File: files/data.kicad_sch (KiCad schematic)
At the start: 2 parts, among them J1 VLB_slot

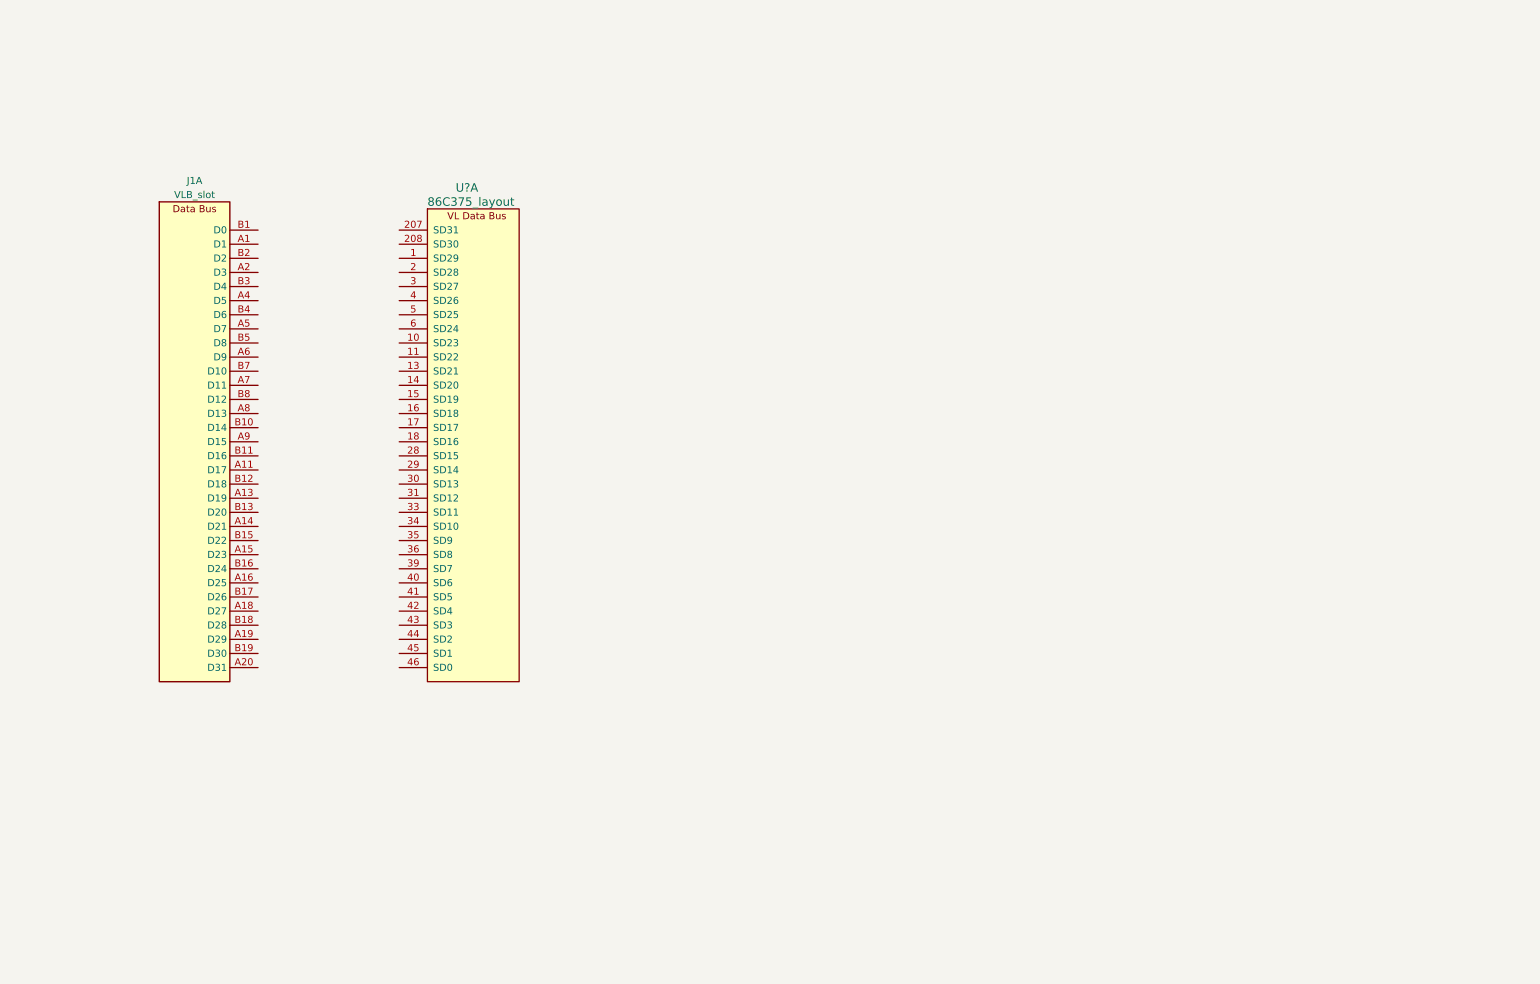
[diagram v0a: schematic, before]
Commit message: work on the memory bus, fixed symbols
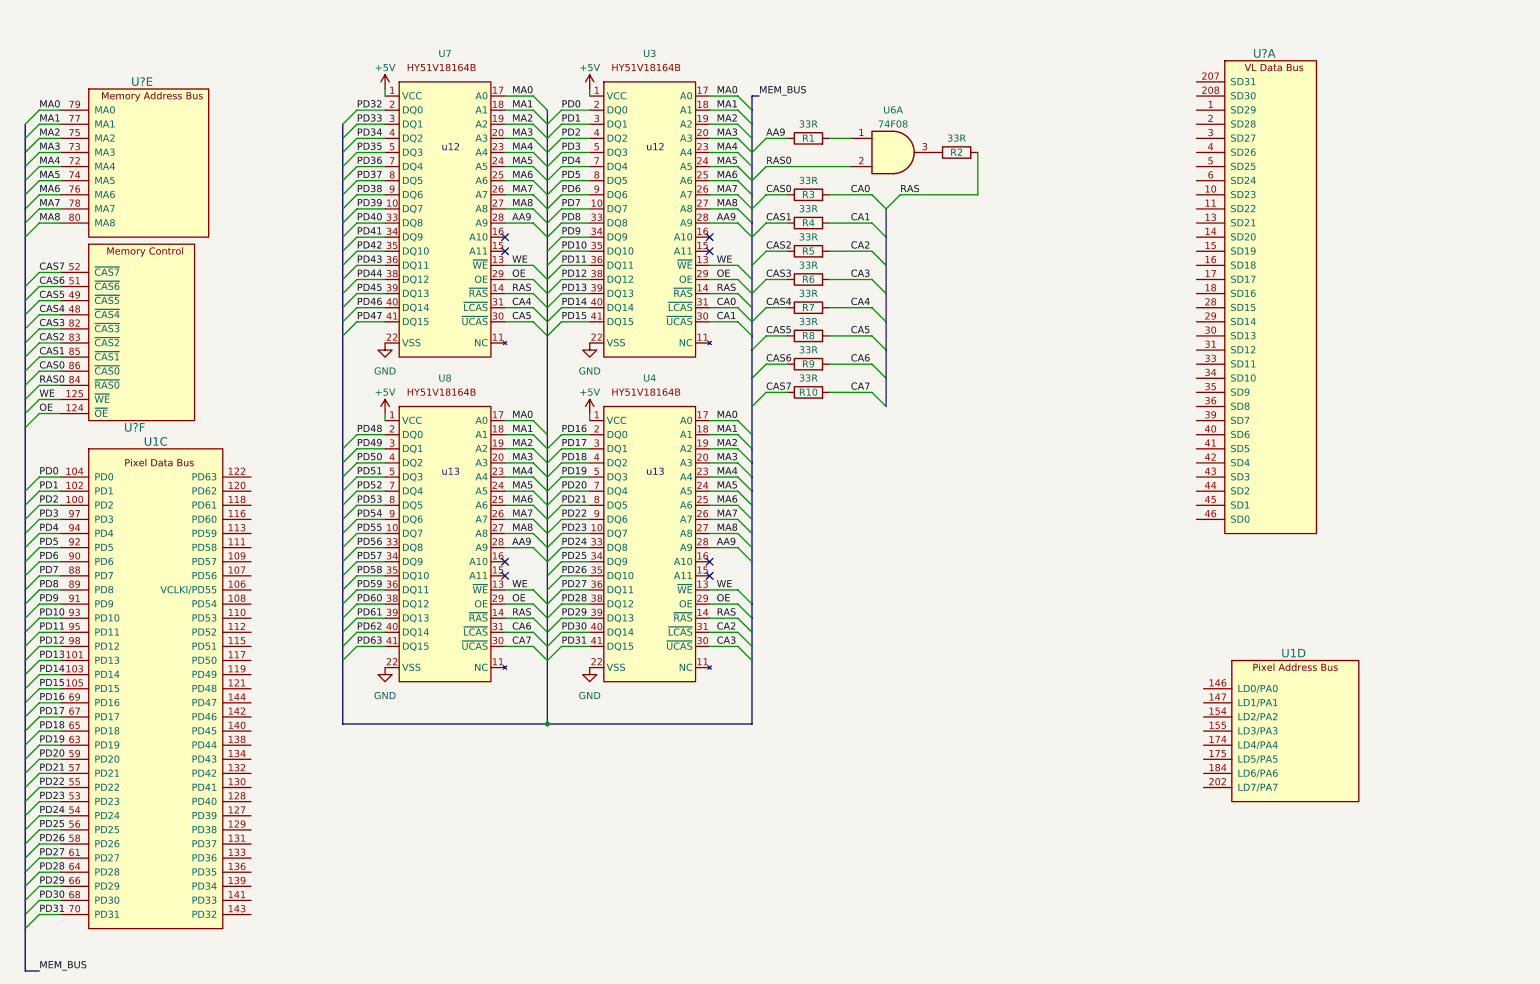
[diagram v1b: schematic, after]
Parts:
- removed J1: VLB_slot, symbol virge:VLB_slot
- added R1, R10, R2, R3, R4, R5, R6, R7, R8, R9: 33R, Resistor_SMD:R_0805_2012Metric, symbol Device:R
- added U1, U? (x2): 86C375_layout, Package_QFP:PQFP-208_28x28mm_P0.5mm, symbol virge:86C375_layout
- added U3, U4, U7, U8: ~, symbol virge:HY51V18164B
- added U6: 74F08, Package_SO:SOIC-14_3.9x8.7mm_P1.27mm, symbol 74xx:74LS08
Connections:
- new net: U7.11 (NC), U7.12 (NC), U7.32 (NC)
- new net: R1.2, U6.1
- new net: R2.1, U6.3
- new net: U4.11 (NC), U4.12 (NC), U4.32 (NC)
- new net: U3.11 (NC), U3.12 (NC), U3.32 (NC)
- new net: U8.11 (NC), U8.12 (NC), U8.32 (NC)
- new net +5V: U3.1 (VCC), U3.21 (VCC), U3.6 (VCC), U4.1 (VCC), U4.21 (VCC), U4.6 (VCC), U7.1 (VCC), U7.21 (VCC), U7.6 (VCC), U8.1 (VCC), U8.21 (VCC), U8.6 (VCC)
- new net AA9: R1.1, U3.28 (A9), U4.28 (A9), U7.28 (A9), U8.28 (A9)
- new net CA0: R3.2, U3.31 (~{LCAS})
- new net CA1: R4.2, U3.30 (~{UCAS})
- new net CA2: R5.2, U4.31 (~{LCAS})
- new net CA3: R6.2, U4.30 (~{UCAS})
- new net CA4: R7.2, U7.31 (~{LCAS})
- new net CA5: R8.2, U7.30 (~{UCAS})
- new net CA6: R9.2, U8.31 (~{LCAS})
- new net CA7: R10.2, U8.30 (~{UCAS})
- new net CAS0: R3.1, U?.86 (~{CAS0})
- new net CAS1: R4.1, U?.85 (~{CAS1})
- new net CAS2: R5.1, U?.83 (~{CAS2})
- new net CAS3: R6.1, U?.82 (~{CAS3})
- new net CAS4: R7.1, U?.48 (~{CAS4})
- new net CAS5: R8.1, U?.49 (~{CAS5})
- new net CAS6: R9.1, U?.51 (~{CAS6})
- new net CAS7: R10.1, U?.52 (~{CAS7})
- new net GND: U3.22 (VSS), U3.37 (VSS), U3.42 (VSS), U4.22 (VSS), U4.37 (VSS), U4.42 (VSS), U7.22 (VSS), U7.37 (VSS), U7.42 (VSS), U8.22 (VSS), U8.37 (VSS), U8.42 (VSS)
- new net MA0: U3.17 (A0), U4.17 (A0), U7.17 (A0), U8.17 (A0), U?.79 (MA0)
- new net MA1: U3.18 (A1), U4.18 (A1), U7.18 (A1), U8.18 (A1), U?.77 (MA1)
- new net MA2: U3.19 (A2), U4.19 (A2), U7.19 (A2), U8.19 (A2), U?.75 (MA2)
- new net MA3: U3.20 (A3), U4.20 (A3), U7.20 (A3), U8.20 (A3), U?.73 (MA3)
- new net MA4: U3.23 (A4), U4.23 (A4), U7.23 (A4), U8.23 (A4), U?.72 (MA4)
- new net MA5: U3.24 (A5), U4.24 (A5), U7.24 (A5), U8.24 (A5), U?.74 (MA5)
- new net MA6: U3.25 (A6), U4.25 (A6), U7.25 (A6), U8.25 (A6), U?.76 (MA6)
- new net MA7: U3.26 (A7), U4.26 (A7), U7.26 (A7), U8.26 (A7), U?.78 (MA7)
- new net MA8: U3.27 (A8), U4.27 (A8), U7.27 (A8), U8.27 (A8), U?.80 (MA8)
- new net OE: U3.29 (OE), U4.29 (OE), U7.29 (OE), U8.29 (OE), U?.124 (~{OE})
- new net PD0: U1.104 (PD0), U3.2 (DQ0)
- new net PD1: U1.102 (PD1), U3.3 (DQ1)
- new net PD10: U1.93 (PD10), U3.35 (DQ10)
- new net PD11: U1.95 (PD11), U3.36 (DQ11)
- new net PD12: U1.98 (PD12), U3.38 (DQ12)
- new net PD13: U1.101 (PD13), U3.39 (DQ13)
- new net PD14: U1.103 (PD14), U3.40 (DQ14)
- new net PD15: U1.105 (PD15), U3.41 (DQ15)
- new net PD16: U1.69 (PD16), U4.2 (DQ0)
- new net PD17: U1.67 (PD17), U4.3 (DQ1)
- new net PD18: U1.65 (PD18), U4.4 (DQ2)
- new net PD19: U1.63 (PD19), U4.5 (DQ3)
- new net PD2: U1.100 (PD2), U3.4 (DQ2)
- new net PD20: U1.59 (PD20), U4.7 (DQ4)
- new net PD21: U1.57 (PD21), U4.8 (DQ5)
- new net PD22: U1.55 (PD22), U4.9 (DQ6)
- new net PD23: U1.53 (PD23), U4.10 (DQ7)
- new net PD24: U1.54 (PD24), U4.33 (DQ8)
- new net PD25: U1.56 (PD25), U4.34 (DQ9)
- new net PD26: U1.58 (PD26), U4.35 (DQ10)
- new net PD27: U1.61 (PD27), U4.36 (DQ11)
- new net PD28: U1.64 (PD28), U4.38 (DQ12)
- new net PD29: U1.66 (PD29), U4.39 (DQ13)
- new net PD3: U1.97 (PD3), U3.5 (DQ3)
- new net PD30: U1.68 (PD30), U4.40 (DQ14)
- new net PD31: U1.70 (PD31), U4.41 (DQ15)
- new net PD32: U7.2 (DQ0)
- new net PD33: U7.3 (DQ1)
- new net PD34: U7.4 (DQ2)
- new net PD35: U7.5 (DQ3)
- new net PD36: U7.7 (DQ4)
- new net PD37: U7.8 (DQ5)
- new net PD38: U7.9 (DQ6)
- new net PD39: U7.10 (DQ7)
- new net PD4: U1.94 (PD4), U3.7 (DQ4)
- new net PD40: U7.33 (DQ8)
- new net PD41: U7.34 (DQ9)
- new net PD42: U7.35 (DQ10)
- new net PD43: U7.36 (DQ11)
- new net PD44: U7.38 (DQ12)
- new net PD45: U7.39 (DQ13)
- new net PD46: U7.40 (DQ14)
- new net PD47: U7.41 (DQ15)
- new net PD48: U8.2 (DQ0)
- new net PD49: U8.3 (DQ1)
- new net PD5: U1.92 (PD5), U3.8 (DQ5)
- new net PD50: U8.4 (DQ2)
- new net PD51: U8.5 (DQ3)
- new net PD52: U8.7 (DQ4)
- new net PD53: U8.8 (DQ5)
- new net PD54: U8.9 (DQ6)
- new net PD55: U8.10 (DQ7)
- new net PD56: U8.33 (DQ8)
- new net PD57: U8.34 (DQ9)
- new net PD58: U8.35 (DQ10)
- new net PD59: U8.36 (DQ11)
- new net PD6: U1.90 (PD6), U3.9 (DQ6)
- new net PD60: U8.38 (DQ12)
- new net PD61: U8.39 (DQ13)
- new net PD62: U8.40 (DQ14)
- new net PD63: U8.41 (DQ15)
- new net PD7: U1.88 (PD7), U3.10 (DQ7)
- new net PD8: U1.89 (PD8), U3.33 (DQ8)
- new net PD9: U1.91 (PD9), U3.34 (DQ9)
- new net RAS: R2.2, U3.14 (~{RAS}), U4.14 (~{RAS}), U7.14 (~{RAS}), U8.14 (~{RAS})
- new net RAS0: U6.2, U?.84 (~{RAS0})
- new net WE: U3.13 (~{WE}), U4.13 (~{WE}), U7.13 (~{WE}), U8.13 (~{WE}), U?.125 (~{WE})
- no-connect marks 0 -> 8
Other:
- note added: "u12"
- note added: "u13"
- moved on the sheet: U?A

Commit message: changed memory chips, more progress
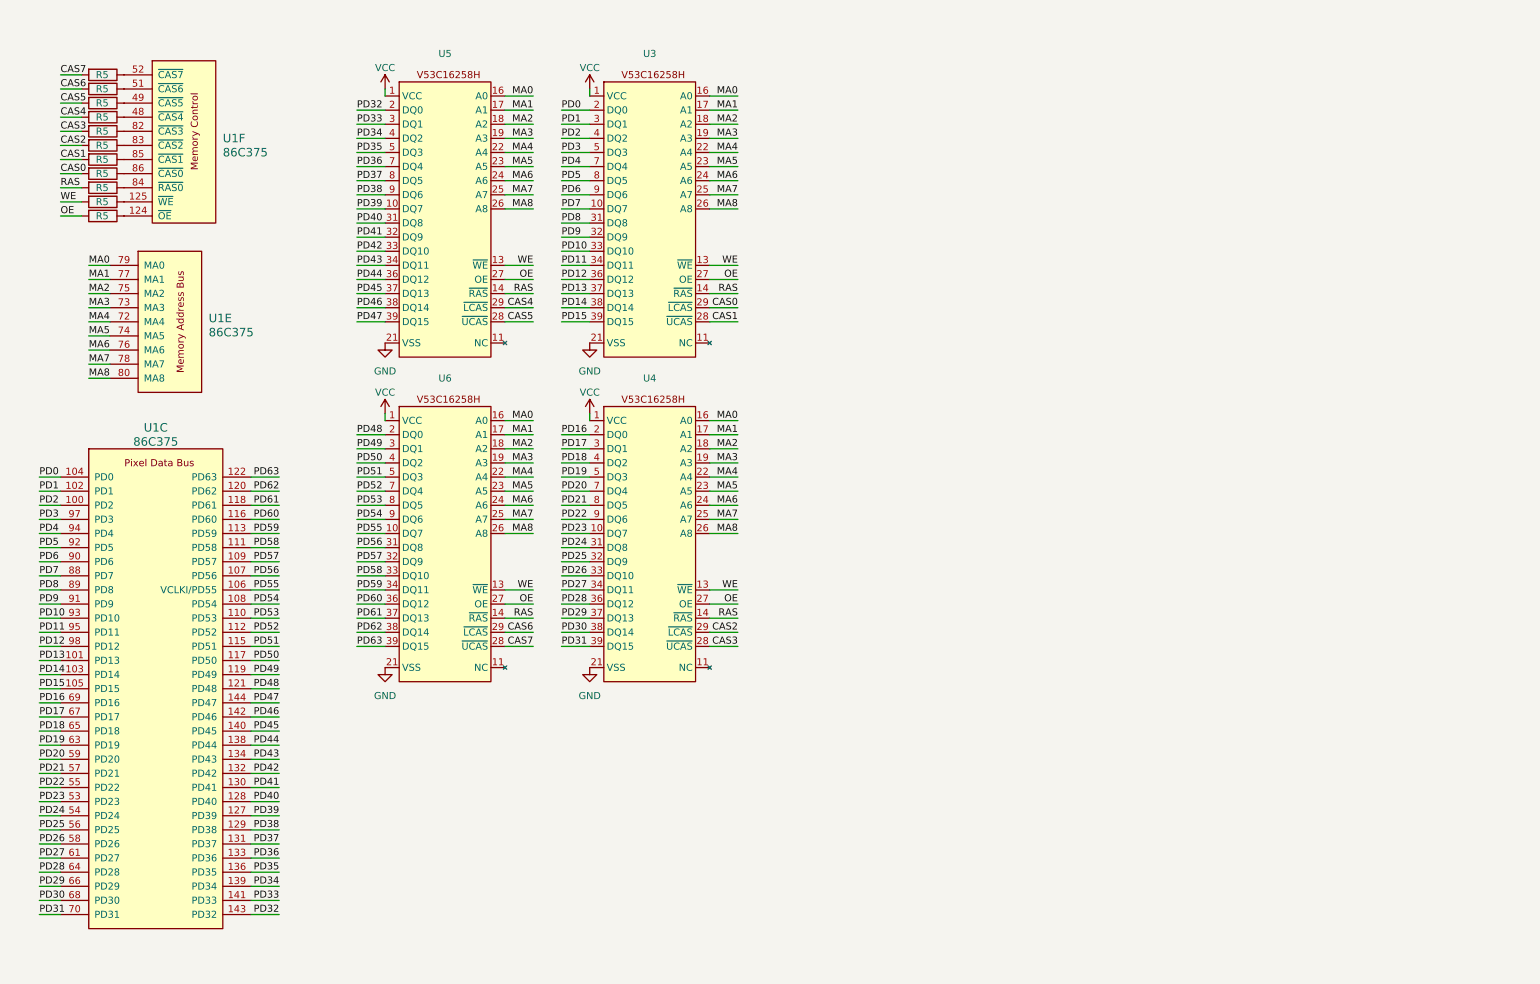
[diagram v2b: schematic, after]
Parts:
- removed R1, R10, R2, R3, R4, R5, R6, R7, R8, R9: 33R, Resistor_SMD:R_0805_2012Metric, symbol Device:R
- removed U1, U? (x3): 86C375_layout, Package_QFP:PQFP-208_28x28mm_P0.5mm, symbol virge:86C375_layout
- removed U6: 74F08, Package_SO:SOIC-14_3.9x8.7mm_P1.27mm, symbol 74xx:74LS08
- removed U7, U8: ~, symbol virge:HY51V18164B
- added R5 (x11): 33R, Resistor_SMD:R_0805_2012Metric_Pad1.20x1.40mm_HandSolder, symbol Device:R
- added U1: 86C375, Package_QFP:PQFP-208_28x28mm_P0.5mm, symbol virge:86C375
- added U5, U6: ~, VLB:SOJ-40_10.16x26.00mm_P1.27mm, symbol virge:HY51V18164B
- U3, U4: footprint (none) -> VLB:SOJ-40_10.16x26.00mm_P1.27mm
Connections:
- net CA0 is gone; now on net PD8: U3.31 (DQ8)
- net CA1 is gone; now on an unnamed net: U3.30 (NC)
- net CA2 is gone; now on net PD24: U4.31 (DQ8)
- net CA3 is gone; now on an unnamed net: U4.30 (NC)
- net CAS0: now also U3.29 (~{LCAS}), R5.2
- net CAS1: now also U3.28 (~{UCAS}), R5.2
- net CAS2: now also U4.29 (~{LCAS}), R5.2
- net CAS3: now also U4.28 (~{UCAS}), R5.2
- net CAS4: now also R5.2, U5.29 (~{LCAS})
- net CAS5: now also R5.2, U5.28 (~{UCAS})
- net CAS6: now also R5.2, U6.29 (~{LCAS})
- net CAS7: now also R5.2, U6.28 (~{UCAS})
- net GND: now also U3.21 (VSS), U3.35 (VSS), U3.40 (VSS), U4.21 (VSS), U4.35 (VSS), U4.40 (VSS), U5.21 (VSS), U5.35 (VSS), U5.40 (VSS), U6.21 (VSS), U6.35 (VSS), U6.40 (VSS); no longer U3.22 (VSS), U3.37 (VSS), U3.42 (VSS), U4.22 (VSS), U4.37 (VSS), U4.42 (VSS)
- net MA0: now also U3.16 (A0), U4.16 (A0), U1.79 (MA0), U5.16 (A0), U6.16 (A0); no longer U3.17 (A0), U4.17 (A0)
- net MA1: now also U3.17 (A1), U4.17 (A1), U1.77 (MA1), U5.17 (A1), U6.17 (A1); no longer U3.18 (A1), U4.18 (A1)
- net MA2: now also U3.18 (A2), U4.18 (A2), U1.75 (MA2), U5.18 (A2), U6.18 (A2); no longer U3.19 (A2), U4.19 (A2)
- net MA3: now also U3.19 (A3), U4.19 (A3), U1.73 (MA3), U5.19 (A3), U6.19 (A3); no longer U3.20 (A3), U4.20 (A3)
- net MA4: now also U3.22 (A4), U4.22 (A4), U1.72 (MA4), U5.22 (A4), U6.22 (A4); no longer U3.23 (A4), U4.23 (A4)
- net MA5: now also U3.23 (A5), U4.23 (A5), U1.74 (MA5), U5.23 (A5), U6.23 (A5); no longer U3.24 (A5), U4.24 (A5)
- net MA6: now also U3.24 (A6), U4.24 (A6), U1.76 (MA6), U5.24 (A6), U6.24 (A6); no longer U3.25 (A6), U4.25 (A6)
- net MA7: now also U3.25 (A7), U4.25 (A7), U1.78 (MA7), U5.25 (A7), U6.25 (A7); no longer U3.26 (A7), U4.26 (A7)
- net MA8: now also U3.26 (A8), U4.26 (A8), U1.80 (MA8), U5.26 (A8), U6.26 (A8); no longer U3.27 (A8), U4.27 (A8)
- net OE: now also U3.27 (OE), U4.27 (OE), R5.2, U5.27 (OE), U6.27 (OE); no longer U3.29 (OE), U4.29 (OE)
- net PD0: now also U1.104 (PD0)
- net PD1: now also U1.102 (PD1)
- net PD10: now also U3.33 (DQ10), U1.93 (PD10); no longer U3.35 (DQ10)
- net PD11: now also U3.34 (DQ11), U1.95 (PD11); no longer U3.36 (DQ11)
- net PD12: now also U3.36 (DQ12), U1.98 (PD12); no longer U3.38 (DQ12)
- net PD13: now also U3.37 (DQ13), U1.101 (PD13); no longer U3.39 (DQ13)
- net PD14: now also U3.38 (DQ14), U1.103 (PD14); no longer U3.40 (DQ14)
- net PD15: now also U3.39 (DQ15), U1.105 (PD15); no longer U3.41 (DQ15)
- net PD16: now also U1.69 (PD16)
- net PD17: now also U1.67 (PD17)
- net PD18: now also U1.65 (PD18)
- net PD19: now also U1.63 (PD19)
- net PD2: now also U1.100 (PD2)
- net PD20: now also U1.59 (PD20)
- net PD21: now also U1.57 (PD21)
- net PD22: now also U1.55 (PD22)
- net PD23: now also U1.53 (PD23)
- net PD24: now also U1.54 (PD24); no longer U4.33 (DQ8)
- net PD25: now also U4.32 (DQ9), U1.56 (PD25); no longer U4.34 (DQ9)
- net PD26: now also U4.33 (DQ10), U1.58 (PD26); no longer U4.35 (DQ10)
- net PD27: now also U4.34 (DQ11), U1.61 (PD27); no longer U4.36 (DQ11)
- net PD28: now also U4.36 (DQ12), U1.64 (PD28); no longer U4.38 (DQ12)
- net PD29: now also U4.37 (DQ13), U1.66 (PD29); no longer U4.39 (DQ13)
- net PD3: now also U1.97 (PD3)
- net PD30: now also U4.38 (DQ14), U1.68 (PD30); no longer U4.40 (DQ14)
- net PD31: now also U4.39 (DQ15), U1.70 (PD31); no longer U4.41 (DQ15)
- net PD32: now also U1.143 (PD32), U5.2 (DQ0)
- net PD33: now also U1.141 (PD33), U5.3 (DQ1)
- net PD34: now also U1.139 (PD34), U5.4 (DQ2)
- net PD35: now also U1.136 (PD35), U5.5 (DQ3)
- net PD36: now also U1.133 (PD36), U5.7 (DQ4)
- net PD37: now also U1.131 (PD37), U5.8 (DQ5)
- net PD38: now also U1.129 (PD38), U5.9 (DQ6)
- net PD39: now also U1.127 (PD39), U5.10 (DQ7)
- net PD4: now also U1.94 (PD4)
- net PD40: now also U1.128 (PD40), U5.31 (DQ8)
- net PD41: now also U1.130 (PD41), U5.32 (DQ9)
- net PD42: now also U1.132 (PD42), U5.33 (DQ10)
- net PD43: now also U1.134 (PD43), U5.34 (DQ11)
- net PD44: now also U1.138 (PD44), U5.36 (DQ12)
- net PD45: now also U1.140 (PD45), U5.37 (DQ13)
- net PD46: now also U1.142 (PD46), U5.38 (DQ14)
- net PD47: now also U1.144 (PD47), U5.39 (DQ15)
- net PD48: now also U1.121 (PD48), U6.2 (DQ0)
- net PD49: now also U1.119 (PD49), U6.3 (DQ1)
- net PD5: now also U1.92 (PD5)
- net PD50: now also U1.117 (PD50), U6.4 (DQ2)
- net PD51: now also U1.115 (PD51), U6.5 (DQ3)
- net PD52: now also U1.112 (PD52), U6.7 (DQ4)
- net PD53: now also U1.110 (PD53), U6.8 (DQ5)
- net PD54: now also U1.108 (PD54), U6.9 (DQ6)
- net PD55: now also U1.106 (VCLKI/PD55), U6.10 (DQ7)
- net PD56: now also U1.107 (PD56), U6.31 (DQ8)
- net PD57: now also U1.109 (PD57), U6.32 (DQ9)
- net PD58: now also U1.111 (PD58), U6.33 (DQ10)
- net PD59: now also U1.113 (PD59), U6.34 (DQ11)
- net PD6: now also U1.90 (PD6)
- net PD60: now also U1.116 (PD60), U6.36 (DQ12)
- net PD61: now also U1.118 (PD61), U6.37 (DQ13)
- net PD62: now also U1.120 (PD62), U6.38 (DQ14)
- net PD63: now also U1.122 (PD63), U6.39 (DQ15)
- net PD7: now also U1.88 (PD7)
- net PD8: now also U1.89 (PD8); no longer U3.33 (DQ8)
- net PD9: now also U3.32 (DQ9), U1.91 (PD9); no longer U3.34 (DQ9)
- net RAS: now also R5.2, U5.14 (~{RAS}), U6.14 (~{RAS})
- net WE: now also R5.2, U5.13 (~{WE}), U6.13 (~{WE})
- net at U4.11 (NC), U4.12 (NC): now also U4.15 (NC); no longer U4.32 (NC)
- net at U3.11 (NC), U3.12 (NC): now also U3.15 (NC); no longer U3.32 (NC)
- net +5V renamed VCC
- net VCC: now also U3.20 (VCC), U4.20 (VCC), U5.1 (VCC), U5.20 (VCC), U5.6 (VCC), U6.1 (VCC), U6.20 (VCC), U6.6 (VCC); no longer U3.21 (VCC), U4.21 (VCC)
- removed net AA9: U3.28 (A9), U4.28 (A9)
- new net: R5.1, U1.84 (~{RAS0})
- new net: R5.1, U1.51 (~{CAS6})
- new net: R5.1, U1.86 (~{CAS0})
- new net: R5.1, U1.49 (~{CAS5})
- new net: R5.1, U1.48 (~{CAS4})
- new net: R5.1, U1.52 (~{CAS7})
- new net: R5.1, U1.125 (~{WE})
- new net: U6.11 (NC), U6.12 (NC), U6.15 (NC), U6.30 (NC)
- new net: R5.1, U1.124 (~{OE})
- new net: R5.1, U1.82 (~{CAS3})
- new net: U5.11 (NC), U5.12 (NC), U5.15 (NC), U5.30 (NC)
- new net: R5.1, U1.83 (~{CAS2})
- new net: R5.1, U1.85 (~{CAS1})
- no-connect marks 8 -> 0
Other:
- note removed: "u12"
- note removed: "u13"

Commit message: even more PCB work
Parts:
- U1: value 86C375 -> 86C325
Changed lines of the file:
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@@
       (effects (font (size 1.524 1.524)) (justify left))
     )
-    (property "Value" "86C375" (at 55.88 39.37 0)
+    (property "Value" "86C325" (at 55.88 39.37 0)
       (effects (font (size 1.524 1.524)) (justify left))
     )
@@
       (effects (font (size 1.524 1.524)))
     )
-    (property "Value" "86C375" (at 43.815 91.44 0)
+    (property "Value" "86C325" (at 43.815 91.44 0)
       (effects (font (size 1.524 1.524)))
     )
@@
       (effects (font (size 1.524 1.524)) (justify left))
     )
-    (property "Value" "86C375" (at 53.34 71.755 0)
+    (property "Value" "86C325" (at 53.34 71.755 0)
       (effects (font (size 1.524 1.524)) (justify left))
     )
